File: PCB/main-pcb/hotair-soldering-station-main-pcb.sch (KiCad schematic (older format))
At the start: 89 parts, among them J1 230VAC_IN, J10 PB6, J11 PB4, J12 PB7, J13 ICP (goldpin r2,54), J2 main-board-conn, J3 EARTH_GND, J4 24V_IN (NS-25 r2,54), J5 PSUPPLY (PWZ-02S r.3,96), J6 HOTAIR_FAN (JST r,2,54)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

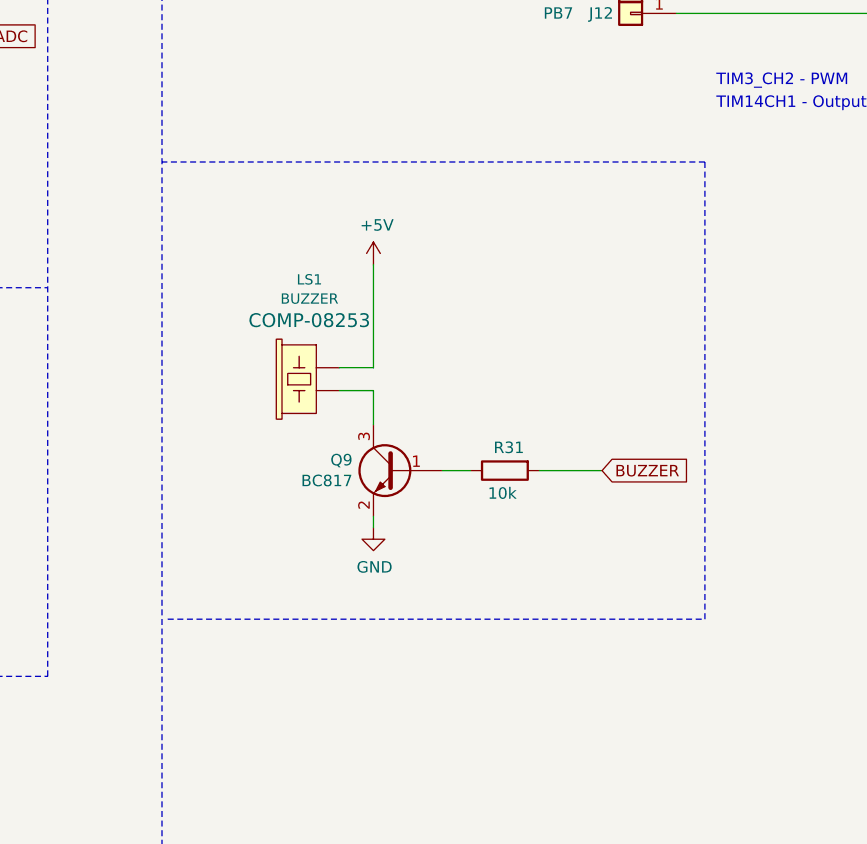
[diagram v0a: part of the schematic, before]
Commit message: LED display, buzzer and PWM done in SW. Some HW bugs fixed.
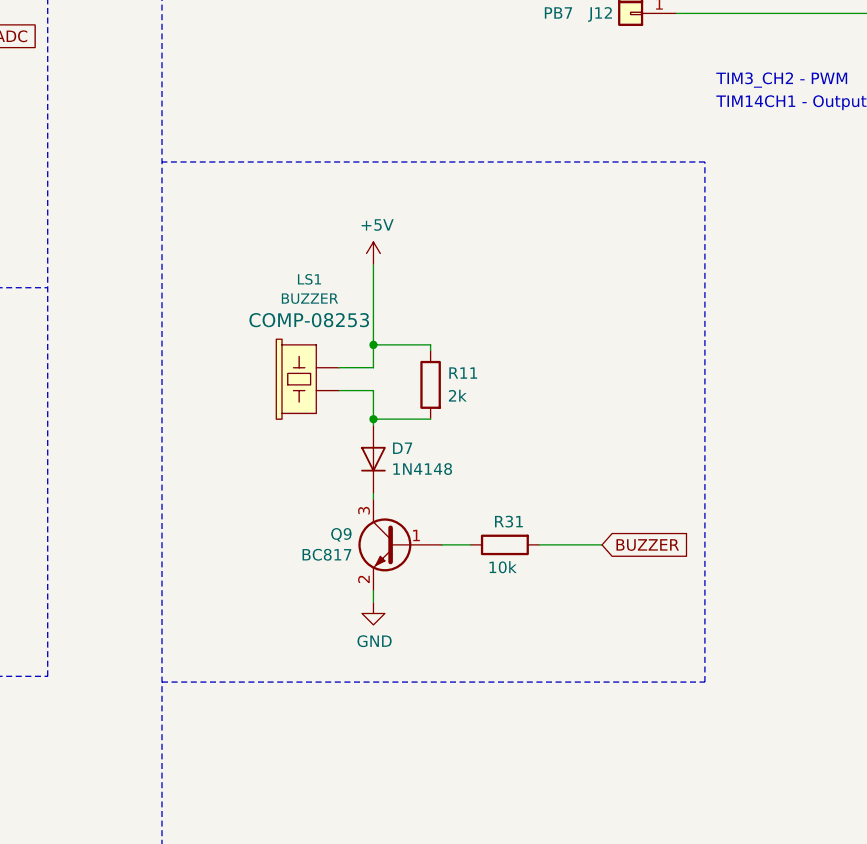
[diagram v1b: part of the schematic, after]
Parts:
- added D7: 1N4148, Diodes_SMD:D_MiniMELF, symbol Device:D
- added R11: 2k, Capacitors:0805, symbol Device:R
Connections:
- net +5V: now also R11.1
- net at LS1.+ (1): now also D7.2 (A), R11.2; no longer Q9.3 (C)
- new net: D7.1 (K), Q9.3 (C)
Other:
- moved on the sheet: Q9, R31
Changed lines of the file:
@@
 L Transistor_BJT:BC817 Q9
 U 1 1 5FA05EA3
-P 14225 11650
-F 0 "Q9" H 14416 11696 50  0000 L CNN
-F 1 "BC817" H 14416 11605 50  0000 L CNN
-F 2 "Package_TO_SOT_SMD:SOT-23" H 14425 11575 50  0001 L CIN
-F 3 "http://www.fairchildsemi.com/ds/BC/BC817.pdf" H 14225 11650 50  0001 L CNN
-	1    14225 11650
+P 14225 11975
+F 0 "Q9" H 14416 12021 50  0000 L CNN
+F 1 "BC817" H 14416 11930 50  0000 L CNN
+F 2 "Package_TO_SOT_SMD:SOT-23" H 14425 11900 50  0001 L CIN
+F 3 "http://www.fairchildsemi.com/ds/BC/BC817.pdf" H 14225 11975 50  0001 L CNN
+	1    14225 11975
 	-1   0    0    -1
 $EndComp
@@
 	13975 11300 14125 11300
 Wire Wire Line
-	14125 11300 14125 11450
+	14125 11300 14125 11425
 $Comp
 L power:GND #PWR0146
 U 1 1 5FA32545
-P 14125 11900
-F 0 "#PWR0146" H 14125 11650 50  0001 C CNN
-F 1 "GND" H 14130 11727 50  0000 C CNN
-F 2 "" H 14125 11900 50  0001 C CNN
-F 3 "" H 14125 11900 50  0001 C CNN
-	1    14125 11900
-	1    0    0    -1
-$EndComp
-Wire Wire Line
-	14125 11900 14125 11850
+P 14125 12225
+F 0 "#PWR0146" H 14125 11975 50  0001 C CNN
+F 1 "GND" H 14130 12052 50  0000 C CNN
+F 2 "" H 14125 12225 50  0001 C CNN
+F 3 "" H 14125 12225 50  0001 C CNN
+	1    14125 12225
+	1    0    0    -1
+$EndComp
+Wire Wire Line
+	14125 12225 14125 12175
 $Comp
 L power:+5V #PWR0147
@@
 	13975 11200 14125 11200
 Wire Wire Line
-	14125 11200 14125 10750
+	14125 11200 14125 11100
 $Comp
 L Device:R R31
 U 1 1 5FA7484A
-P 14700 11650
-F 0 "R31" V 14600 11700 50  0000 R CNN
-F 1 "10k" V 14800 11725 50  0000 R CNN
-F 2 "Capacitors:0805" V 14630 11650 50  0001 C CNN
-F 3 "~" H 14700 11650 50  0001 C CNN
-	1    14700 11650
+P 14700 11975
+F 0 "R31" V 14600 12025 50  0000 R CNN
+F 1 "10k" V 14800 12050 50  0000 R CNN
+F 2 "Capacitors:0805" V 14630 11975 50  0001 C CNN
+F 3 "~" H 14700 11975 50  0001 C CNN
+	1    14700 11975
 	0    -1   1    0
 $EndComp
 Wire Wire Line
-	14550 11650 14425 11650
-Wire Wire Line
-	14850 11650 15125 11650
-Text GLabel 15125 11650 2    50   Input ~ 0
+	14550 11975 14425 11975
+Wire Wire Line
+	14850 11975 15125 11975
+Text GLabel 15125 11975 2    50   Input ~ 0
 BUZZER
 Wire Notes Line
-	13225 12300 15575 12300
+	13200 12575 15575 12575
 Wire Notes Line
-	15575 12300 15575 10300
+	15575 12575 15575 10300
 Wire Notes Line
 	15575 10300 13200 10300
@@
 Text Notes 3925 2200 0    50   ~ 0
 FB resistor in module: 43k
+$Comp
+L Device:R R11
+U 1 1 5FF3E3A2
+P 14375 11275
+F 0 "R11" H 14300 11325 50  0000 R CNN
+F 1 "2k" H 14300 11225 50  0000 R CNN
+F 2 "Capacitors:0805" V 14305 11275 50  0001 C CNN
+F 3 "~" H 14375 11275 50  0001 C CNN
+	1    14375 11275
+	-1   0    0    -1
+$EndComp
+$Comp
+L Device:D D7
+U 1 1 5FF5FA4A
+P 14125 11600
+F 0 "D7" V 14171 11521 50  0000 R CNN
+F 1 "1N4148" V 14080 11521 50  0000 R CNN
+F 2 "Diodes_SMD:D_MiniMELF" H 14125 11600 50  0001 C CNN
+F 3 "~" H 14125 11600 50  0001 C CNN
+	1    14125 11600
+	0    -1   -1   0
+$EndComp
+Wire Wire Line
+	14125 11775 14125 11750
+Wire Wire Line
+	14375 11125 14375 11100
+Wire Wire Line
+	14375 11100 14125 11100
+Connection ~ 14125 11100
+Wire Wire Line
+	14125 11100 14125 10750
+Wire Wire Line
+	14375 11425 14125 11425
+Connection ~ 14125 11425
+Wire Wire Line
+	14125 11425 14125 11450
 $EndSCHEMATC

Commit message: Fan DC converter new design, ADC and PWM done
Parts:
- removed C9: 47u/35V, Capacitor_THT:CP_Radial_D6.3mm_P2.50mm, symbol Device:CP
- removed D2: 1N4148, Diodes_SMD:D_MiniMELF, symbol Diode:1N4148
- removed J12: PB7, My-Footprints:WIRE_PAD_1,3mm, symbol Connector_Generic:Conn_01x01
- removed Q3: BC817, Package_TO_SOT_SMD:SOT-23, symbol Transistor_BJT:BC817
- removed Q4: BC807, Package_TO_SOT_SMD:SOT-23, symbol Transistor_BJT:BC807
- removed Q5: IRLIZ44N, TO_SOT_Packages_SMD:TO-252-2, symbol Transistor_FET:IRLIZ44N
- added C9: 10n, Capacitors:0805, symbol Device:C
- added D2: MBR052, Diodes_SMD:D_SOD-123, symbol Diode:1N5819
- added D8: 3V6, Diodes_SMD:D_MiniMELF, symbol Device:D_Zener
- added Q3: BC327, My-Footprints:TO-92_Inline_Wide, symbol Transistor_BJT:BC327
- added R14: 24k, Capacitors:0805, symbol Device:R
- added R26, R36: 1k, Capacitors:0805, symbol Device:R
- added R35: 4k7, Capacitors:0805, symbol Device:R
- C3: footprint Capacitor_THT:CP_Radial_D10.0mm_P3.80mm -> Capacitor_THT:CP_Radial_D6.3mm_P2.50mm
- C6: value 1u -> 10n; footprint Capacitors:1206 -> Capacitors:0805
- R8: value 4k7 -> 2k2
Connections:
- net +24V: now also Q3.3 (E), R35.2
- net FAN_SUPPLY: now also R14.2
- net GND: now also C9.1, D8.2 (A), R26.1
- net HOTAIR_HEATER_CTRL: now also U5.30 (PB7); no longer U5.9 (PA3)
- net at D3.1 (K), L1.1: now also D2.2 (A), Q3.1 (C); no longer C6.1
- net at D1.1 (K), Q2.3 (C), R8.2: now also C6.1
- net at C6.2, R8.1: now also D2.1 (K), Q3.2 (B), R35.1
- new net: C9.2, D8.1 (K), R14.1, R26.2, R36.1
- new net FAN_ADC: R36.2, U5.9 (PA3)
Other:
- moved on the sheet: C2, C3, C8, D1, D3, L1, Q2, R1, R4, R8
